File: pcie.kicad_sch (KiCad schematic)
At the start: 38 parts, among them U15 XC7K160T-FFG676

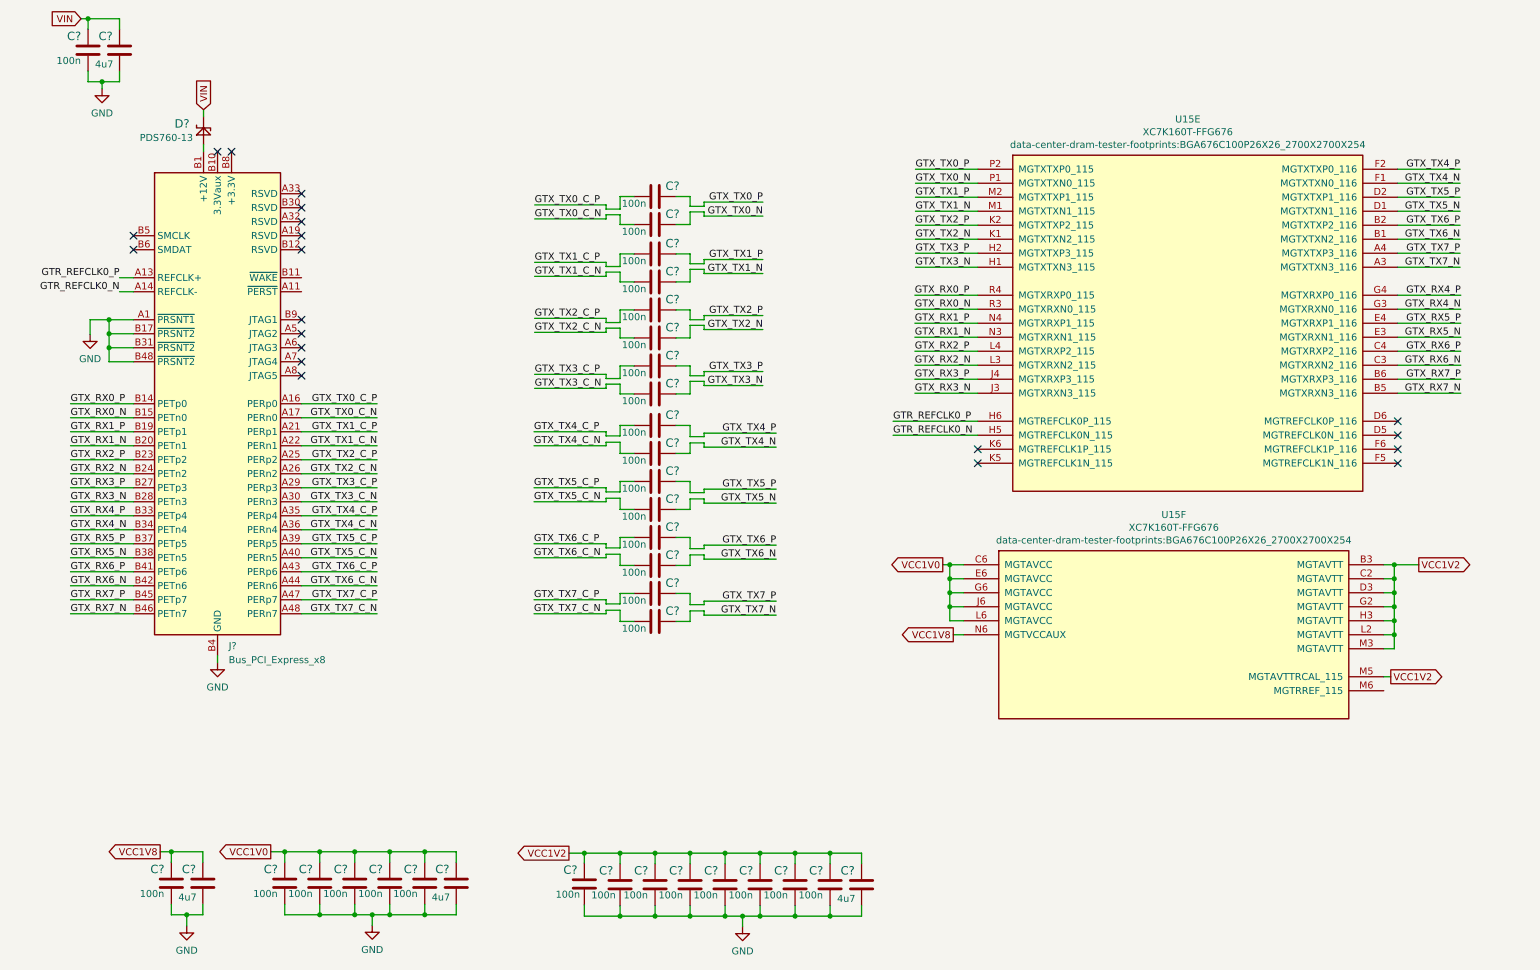
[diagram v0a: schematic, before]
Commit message: For PCIe: added MGTAVTT calibration resistor, proper HCSL temination, REFCLK AC decoupling, PERST connection, corrected PRSNT1 to PRSNT2 connection.
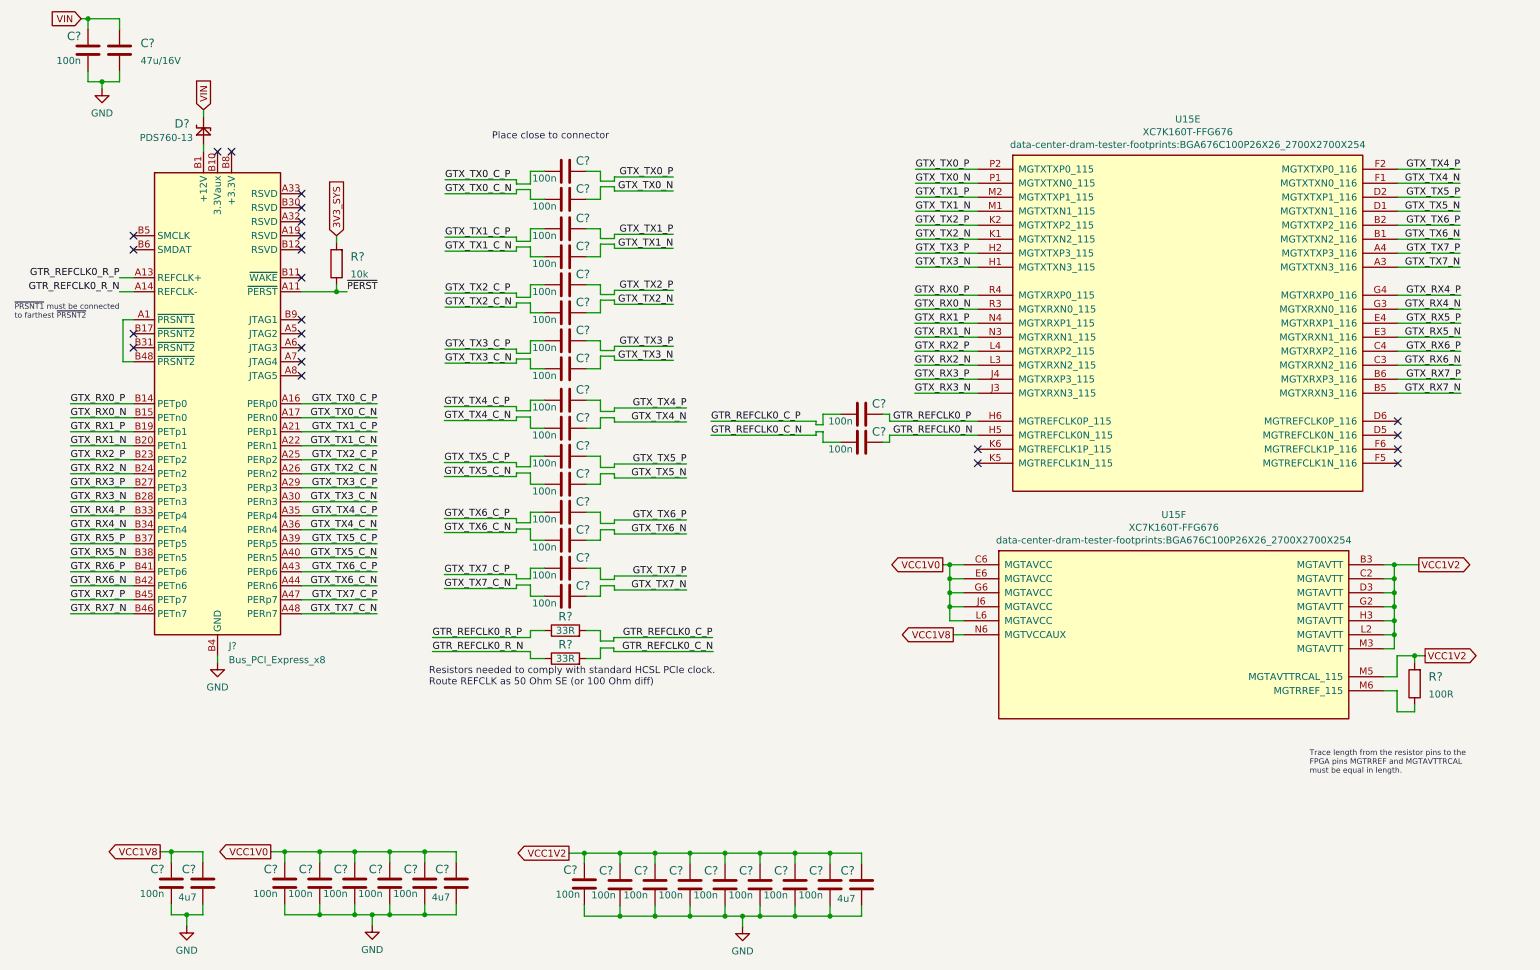
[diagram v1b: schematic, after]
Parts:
- removed C?: C_4u7_0402, antmicro-footprints:0402-cap, symbol antmicroCapacitors0402:C_4u7_0402
- added C? (x2): C_100n_0402, antmicro-footprints:0402-cap, symbol antmicroCapacitors0402:C_100n_0402
- added C?: C_47u_16V_1206, antmicro-footprints:1206-cap, symbol antmicroCapacitorsmisc:C_47u_16V_1206
- added R?: R_10k_0402, antmicro-footprints:0402-res, symbol antmicroResistors0402:R_10k_0402
- added R? (x2): R_33R_0402, antmicro-footprints:0402-res, symbol antmicroResistors0402:R_33R_0402
- added R?: R_100R_0402, antmicro-footprints:0402-res, symbol antmicroResistors0402:R_100R_0402
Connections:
- net GND: now also C?.2; no longer J?.A1 (~{PRSNT1}), J?.B17 (~{PRSNT2}), J?.B31 (~{PRSNT2}), J?.B48 (~{PRSNT2})
- net GTR_REFCLK0_N: now also C?.2; no longer J?.A14 (REFCLK-)
- net GTR_REFCLK0_P: now also C?.2; no longer J?.A13 (REFCLK+)
- net VCC1V2: now also R?.2
- net VIN: now also C?.1
- net ~{PERST}: now reaches J?.A11 (~{PERST})
- net ~{PERST}: now also R?.1
- net at U15.M6 (MGTRREF_115): now also R?.1
- new net: J?.A1 (~{PRSNT1}), J?.B48 (~{PRSNT2})
- new net 3V3_SYS: R?.2
- new net GTR_REFCLK0_C_N: C?.1, R?.2
- new net GTR_REFCLK0_C_P: C?.1, R?.2
- new net GTR_REFCLK0_R_N: J?.A14 (REFCLK-), R?.1
- new net GTR_REFCLK0_R_P: J?.A13 (REFCLK+), R?.1
- no-connect marks 20 -> 23
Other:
- note added: "Place close to connector"
- note added: "Resistors needed to comply with standard HCSL PCIe clock. Route REFCLK as 50 Ohm SE (or 100 Ohm diff)"
- note added: "Trace length from the resistor pins to the FPGA pins MGTRREF and MGTAVTTRCAL must be equal in length."
- note added: "~{PRSNT1} must be connected to farthest ~{PRSNT2}"
- moved on the sheet: C?

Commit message: B2B FMC HPC connector added, recconected PCIe to new connector, added ETH mux
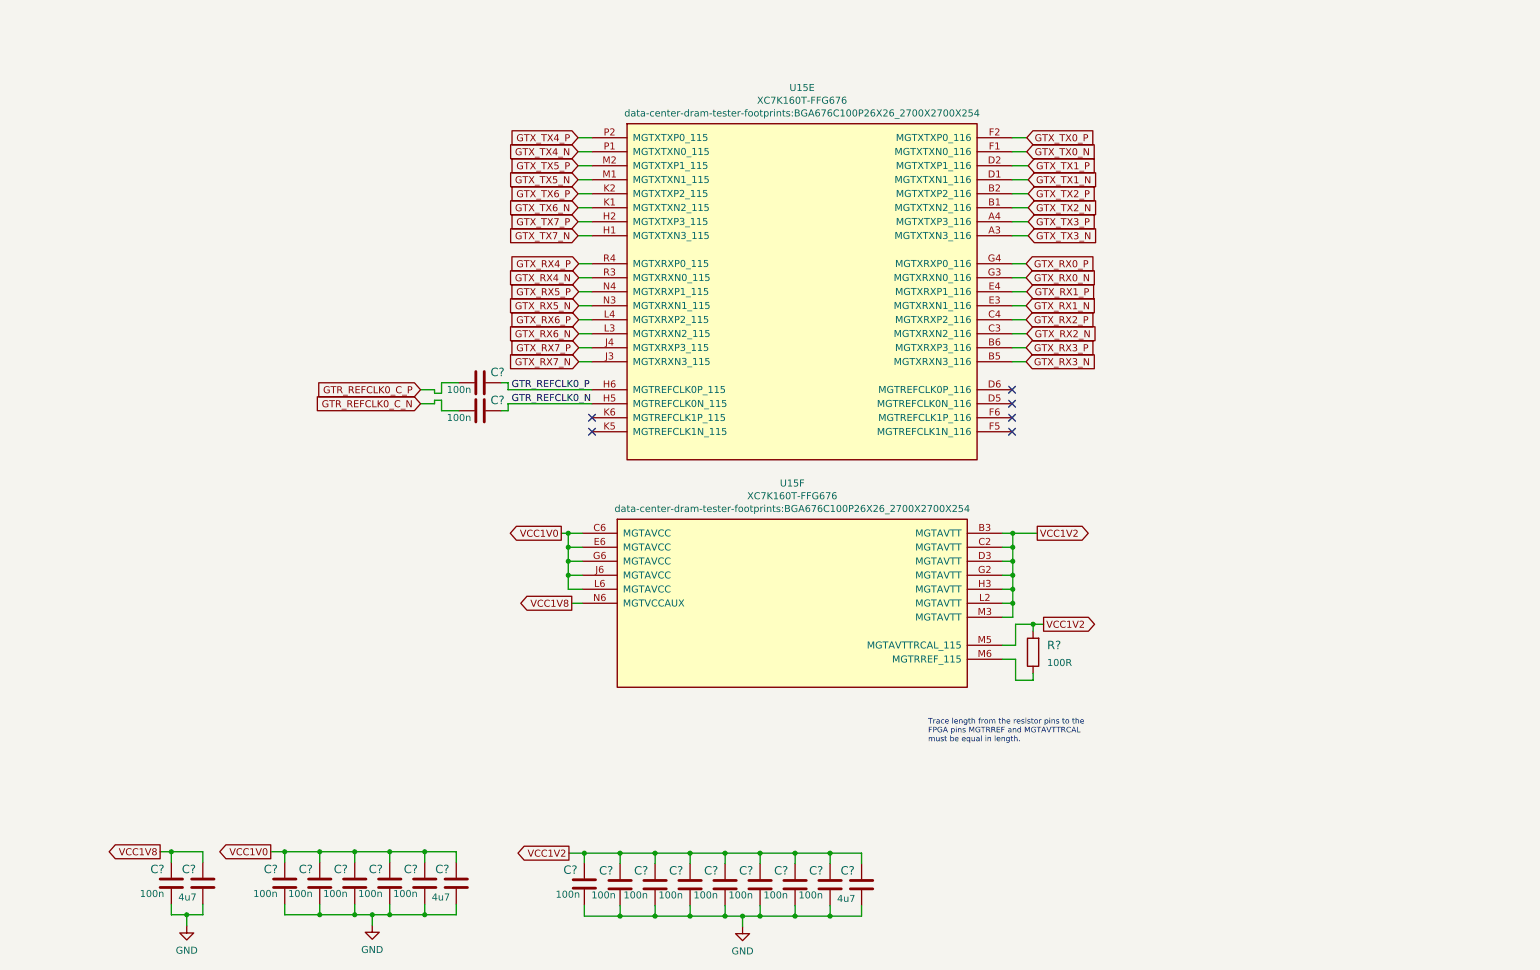
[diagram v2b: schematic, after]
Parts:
- removed C? (x16): C_100n_0402, antmicro-footprints:0402-cap, symbol antmicroCapacitors0402:C_100n_0402
- removed C?: C_100n_0201, antmicro-footprints:0201-res, symbol antmicroCapacitorsmisc:C_100n_0201
- removed C?: C_47u_16V_1206, antmicro-footprints:1206-cap, symbol antmicroCapacitorsmisc:C_47u_16V_1206
- removed D?: PDS760-13, data-center-dram-tester-footprints:PDS760-13, symbol data-center-dram-tester:PDS760-13
- removed J?: Bus_PCI_Express_x8, Connector_PCBEdge:BUS_PCIexpress_x8, symbol Connector:Bus_PCI_Express_x8
- removed R?: R_10k_0402, antmicro-footprints:0402-res, symbol antmicroResistors0402:R_10k_0402
- removed R? (x2): R_33R_0402, antmicro-footprints:0402-res, symbol antmicroResistors0402:R_33R_0402
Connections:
- net GTX_RX0_N: now also U15.G3 (MGTXRXN0_116); no longer U15.R3 (MGTXRXN0_115)
- net GTX_RX0_P: now also U15.G4 (MGTXRXP0_116); no longer U15.R4 (MGTXRXP0_115)
- net GTX_RX1_N: now also U15.E3 (MGTXRXN1_116); no longer U15.N3 (MGTXRXN1_115)
- net GTX_RX1_P: now also U15.E4 (MGTXRXP1_116); no longer U15.N4 (MGTXRXP1_115)
- net GTX_RX2_N: now also U15.C3 (MGTXRXN2_116); no longer U15.L3 (MGTXRXN2_115)
- net GTX_RX2_P: now also U15.C4 (MGTXRXP2_116); no longer U15.L4 (MGTXRXP2_115)
- net GTX_RX3_N: now also U15.B5 (MGTXRXN3_116); no longer U15.J3 (MGTXRXN3_115)
- net GTX_RX3_P: now also U15.B6 (MGTXRXP3_116); no longer U15.J4 (MGTXRXP3_115)
- net GTX_RX4_N: now also U15.R3 (MGTXRXN0_115); no longer U15.G3 (MGTXRXN0_116)
- net GTX_RX4_P: now also U15.R4 (MGTXRXP0_115); no longer U15.G4 (MGTXRXP0_116)
- net GTX_RX5_N: now also U15.N3 (MGTXRXN1_115); no longer U15.E3 (MGTXRXN1_116)
- net GTX_RX5_P: now also U15.N4 (MGTXRXP1_115); no longer U15.E4 (MGTXRXP1_116)
- net GTX_RX6_N: now also U15.L3 (MGTXRXN2_115); no longer U15.C3 (MGTXRXN2_116)
- net GTX_RX6_P: now also U15.L4 (MGTXRXP2_115); no longer U15.C4 (MGTXRXP2_116)
- net GTX_RX7_N: now also U15.J3 (MGTXRXN3_115); no longer U15.B5 (MGTXRXN3_116)
- net GTX_RX7_P: now also U15.J4 (MGTXRXP3_115); no longer U15.B6 (MGTXRXP3_116)
- net GTX_TX0_N: now also U15.F1 (MGTXTXN0_116); no longer U15.P1 (MGTXTXN0_115)
- net GTX_TX0_P: now also U15.F2 (MGTXTXP0_116); no longer U15.P2 (MGTXTXP0_115)
- net GTX_TX1_N: now also U15.D1 (MGTXTXN1_116); no longer U15.M1 (MGTXTXN1_115)
- net GTX_TX1_P: now also U15.D2 (MGTXTXP1_116); no longer U15.M2 (MGTXTXP1_115)
- net GTX_TX2_N: now also U15.B1 (MGTXTXN2_116); no longer U15.K1 (MGTXTXN2_115)
- net GTX_TX2_P: now also U15.B2 (MGTXTXP2_116); no longer U15.K2 (MGTXTXP2_115)
- net GTX_TX3_N: now also U15.A3 (MGTXTXN3_116); no longer U15.H1 (MGTXTXN3_115)
- net GTX_TX3_P: now also U15.A4 (MGTXTXP3_116); no longer U15.H2 (MGTXTXP3_115)
- net GTX_TX4_N: now also U15.P1 (MGTXTXN0_115); no longer U15.F1 (MGTXTXN0_116)
- net GTX_TX4_P: now also U15.P2 (MGTXTXP0_115); no longer U15.F2 (MGTXTXP0_116)
- net GTX_TX5_N: now also U15.M1 (MGTXTXN1_115); no longer U15.D1 (MGTXTXN1_116)
- net GTX_TX5_P: now also U15.M2 (MGTXTXP1_115); no longer U15.D2 (MGTXTXP1_116)
- net GTX_TX6_N: now also U15.K1 (MGTXTXN2_115); no longer U15.B1 (MGTXTXN2_116)
- net GTX_TX6_P: now also U15.K2 (MGTXTXP2_115); no longer U15.B2 (MGTXTXP2_116)
- net GTX_TX7_N: now also U15.H1 (MGTXTXN3_115); no longer U15.A3 (MGTXTXN3_116)
- net GTX_TX7_P: now also U15.H2 (MGTXTXP3_115); no longer U15.A4 (MGTXTXP3_116)
- no-connect marks 23 -> 6
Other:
- note removed: "Place close to connector"
- note removed: "Resistors needed to comply with standard HCSL PCIe clock. Route REFCLK as 50 Ohm SE (or 100 Ohm diff)"
- note removed: "~{PRSNT1} must be connected to farthest ~{PRSNT2}"
- moved on the sheet: C?, R?, U15E, U15F
